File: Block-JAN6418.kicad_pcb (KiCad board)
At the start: 2 copper layers, 65 x 65 mm, 21 parts, among them J1 B+, J2 Sig_gnd, J3 Sig_in, J4 Sig_out, J5 9V, U1 JAN6418, U2 LM317L

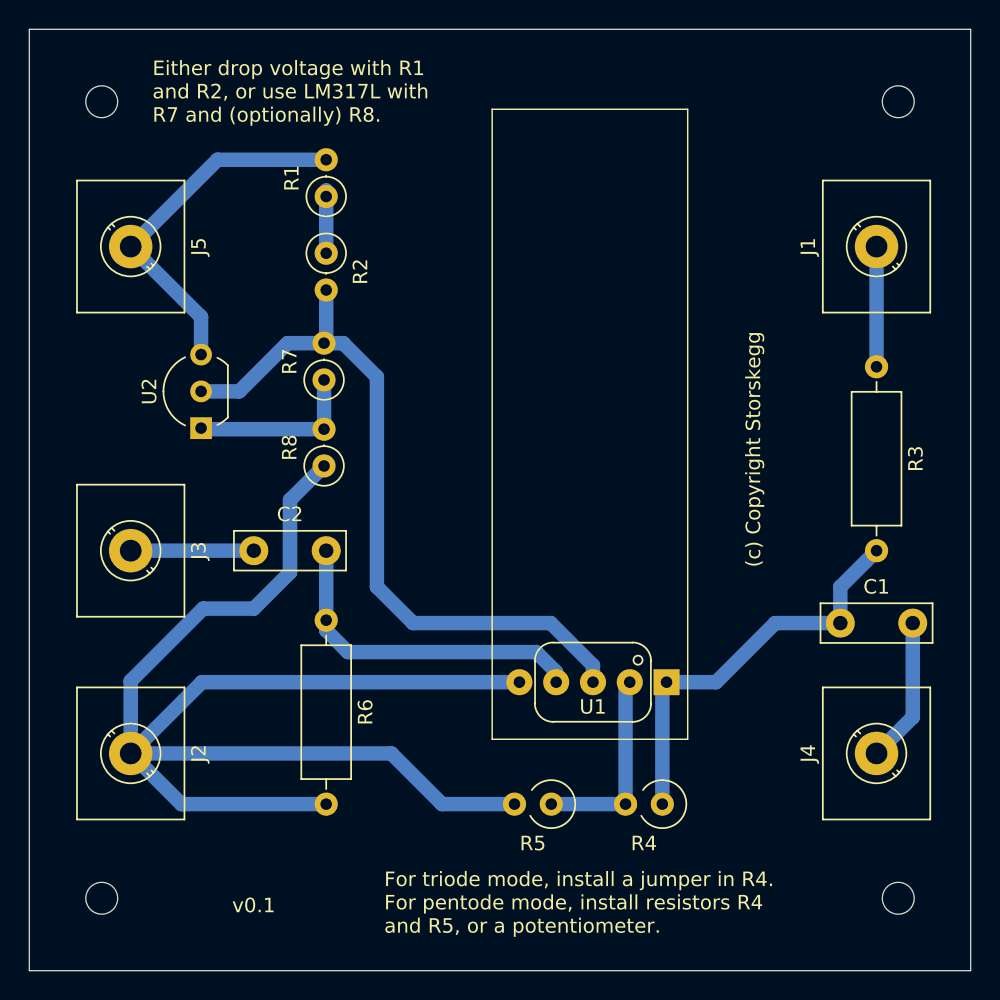
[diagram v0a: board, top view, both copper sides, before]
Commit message: narrow the board, and add some additional silkscreening
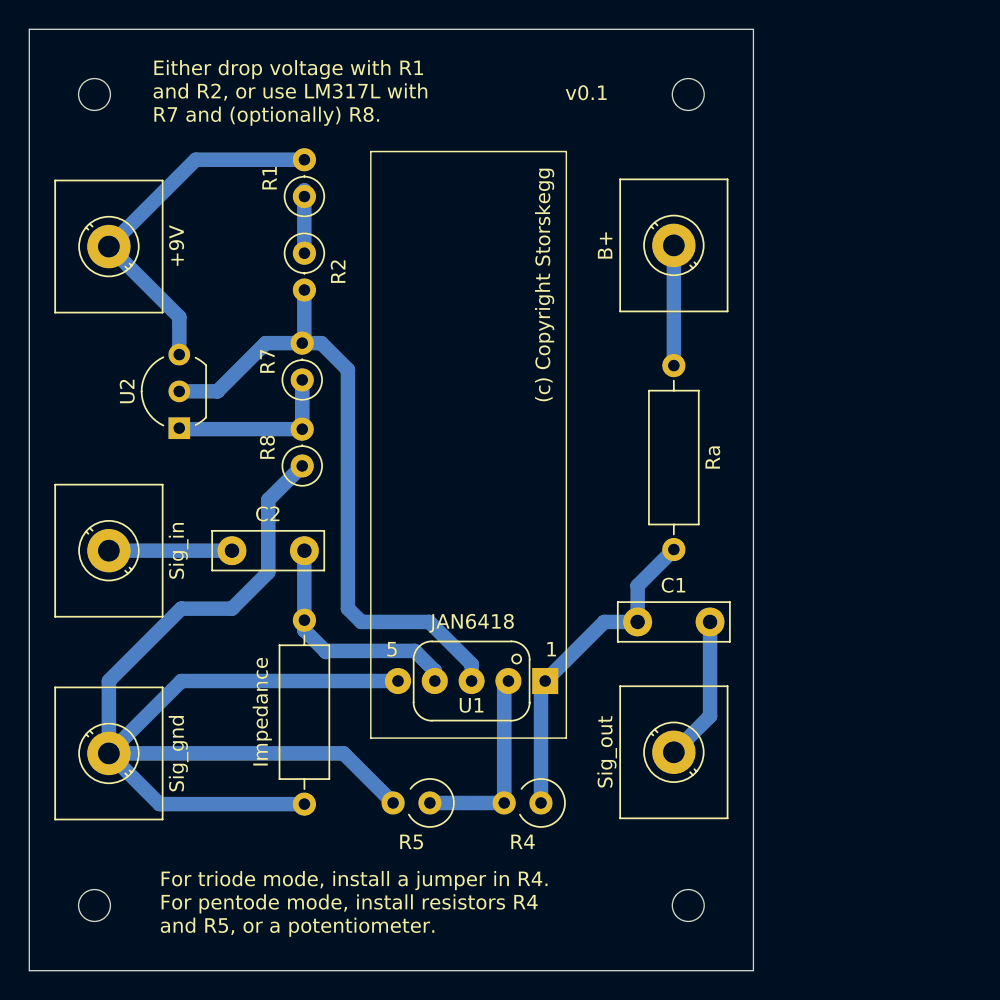
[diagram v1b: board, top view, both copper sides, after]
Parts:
- moved REF** 14.5 mm to (95.5, 39.5)
- moved REF** 14.5 mm to (95.5, 95.5)
- moved B+ 14.0 mm to (94.5, 49.9)
- moved C1 14.0 mm to (92.0, 75.9)
- moved Ra 14.0 mm to (94.5, 58.2)
- moved Sig_out 14.0 mm to (94.5, 84.9)
- moved R5 8.38 mm to (77.7, 88.4)
- moved R4 8.38 mm to (85.3, 88.4)
- moved U1 8.38 mm to (85.6, 80.0)
- moved +9V 1.51 mm to (55.5, 50.0)
- moved C2 1.51 mm to (64.0, 71.0)
- moved Sig_gnd 1.51 mm to (55.5, 85.0)
- moved Sig_in 1.51 mm to (55.5, 71.0)
- moved U2 1.51 mm to (60.4, 62.5)
- moved Impedance 1.50 mm to (69.0, 75.8)
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- renumbered J5 to +9V, J1 to B+, R6 to Impedance, R3 to Ra, J2 to Sig_gnd, J3 to Sig_in, J4 to Sig_out
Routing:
- net GND: track 99.2 -> 85.5 mm
- net Net-(U1A-G1): track 23.1 -> 16.2 mm
- net Net-(U2-VO): track 51.0 -> 45.3 mm
- net Net-(U1A-P): track 28.3 -> 22.7 mm
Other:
- board size 65 x 65 mm -> 50 x 65 mm
- board text added: "1"
- board text added: "5"
- board text added: "JAN6418"

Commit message: shrinkage
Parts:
- moved R8 6.45 mm to (62.5, 64.0)
- moved R7 5.80 mm to (63.5, 57.0), turned to 180 degrees
- moved U2 5.10 mm to (55.4, 61.5)
- moved R4 4.16 mm to (83.0, 85.0)
- moved R5 4.06 mm to (75.5, 85.0)
- moved R1 3.95 mm to (65.0, 46.5), turned to 180 degrees
- moved R2 3.95 mm to (65.0, 50.4)
- moved U1 3.04 mm to (83.0, 78.5)
- moved Impedance 2.66 mm to (67.5, 73.6)
- moved B+ 2.53 mm to (92.5, 48.4)
- moved C1 2.53 mm to (90.0, 74.4)
- moved Ra 2.53 mm to (92.5, 56.7)
- moved Sig_out 2.53 mm to (92.5, 83.4)
- moved C2 2.15 mm to (62.5, 69.5)
- moved REF** 2.12 mm to (94.0, 94.0)
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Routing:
- net +9V: track 25.5 -> 15.7 mm
- net GND: track 85.5 -> 76.4 mm
- net Net-(U1A-G2): track 13.7 -> 11.4 mm
- net Net-(U1A-G1): track 16.2 -> 14.7 mm
- net Net-(J3-Pin_1): track 8.50 -> 7.01 mm
- net Net-(U1A-P): track 22.7 -> 21.2 mm
- net Net-(U2-VO): track 45.3 -> 46.2 mm
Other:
- board size 50 x 65 mm -> 48 x 63 mm
- board text added: "Either drop voltage with R1 and R2, OR use LM317L with R7 and (optionally) R8."
- board text added: "v0.3"
- board text removed: "Either drop voltage with R1 and R2, or use LM317L with R7 and (optionally) R8."
- board text removed: "v0.1"

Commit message: bigger change...
1. Added L1 Ground Plane
2. Added filter and bandpass capacitors to LM317L optional block
3. `Sig_in` and `Sig_gnd` swapped physical locations...
    1. `Sig_gnd` is now closer to PSU block ground connections (lower
       impedance ground paths)
    2. `Sig_gnd` now closer to `R_impedance` ground connection
    3. `Sig_gnd` distance to `JAN6418` ground pin is about unchanged
4. Other general changes and general notes
    1. Valve heater power now routed further away from valve body
    2. Power blocks now a bit more compact, and further away from valve
       body
    3. No impeded ground paths on the ground plane (e.g. no going around
       vias, pins, etc; all straight line paths to `Sig_gnd`)
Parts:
- added C3: 100nF, Capacitor_THT:C_Rect_L4.6mm_W2.0mm_P2.50mm_MKS02_FKP02, F.Cu at (53.0, 61.8)
- added C4: 1uF, Capacitor_THT:CP_Radial_D4.0mm_P1.50mm, F.Cu at (58.0, 62.3)
- moved C2 16.5 mm to (62.5, 86.0)
- moved Sig_in 14.0 mm to (55.5, 83.5)
- moved Sig_gnd 12.5 mm to (55.5, 71.0)
- moved Impedance 9.58 mm to (65.0, 82.8), turned to 90 degrees
- moved U2 5.11 mm to (58.0, 57.1), turned to 180 degrees
- moved R2 1.67 mm to (64.5, 52.0), turned to 180 degrees
- moved R1 1.63 mm to (64.5, 48.0)
- moved R7 1.59 mm to (63.5, 58.5), turned to 90 degrees
- moved R8 1.00 mm to (63.5, 64.0)
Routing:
- net GND: track 76.4 -> 0.00 mm
- net Net-(U2-VO): track 46.2 -> 53.4 mm
- net +9V: track 15.7 -> 20.4 mm
- net Net-(U2-ADJ): track 12.0 -> 9.00 mm
- net Net-(U1A-G1): track 14.7 -> 16.2 mm
- net Net-(J3-Pin_1): track 7.01 -> 8.04 mm
- added copper zone on F.Cu, net GND
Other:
- board text added: "v0.5a"
- board text removed: "v0.3"

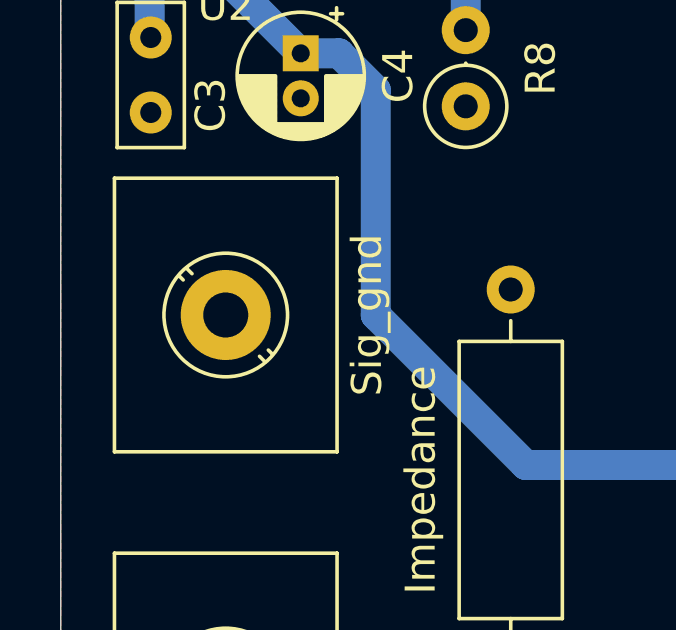
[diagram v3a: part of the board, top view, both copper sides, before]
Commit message: lower impedance of sig_gnd connection
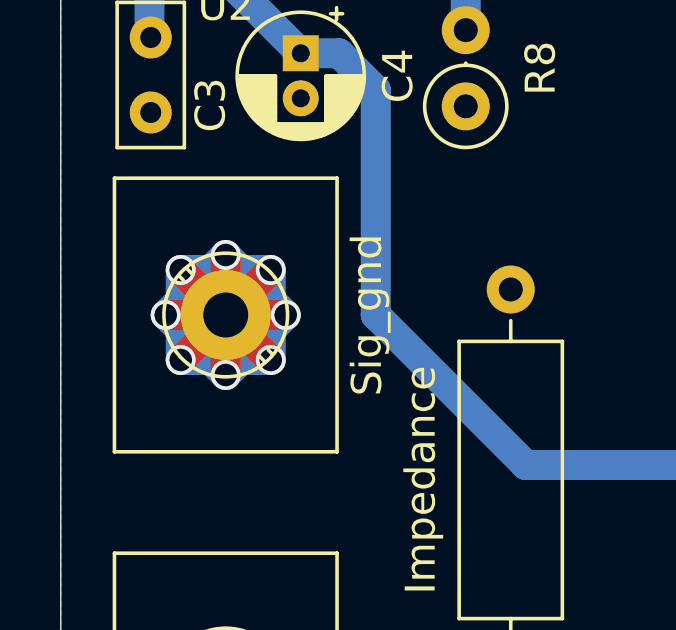
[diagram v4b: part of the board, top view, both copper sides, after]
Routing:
- net GND: track 0.00 -> 30.1 mm, vias 0 -> 8
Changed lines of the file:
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@@
+	)
+	(segment
+		(start 55.5 71)
+		(end 55.5 73)
+		(width 1)
+		(layer "F.Cu")
+		(net 6)
+	)
+	(segment
+		(start 55.5 71)
+		(end 54 72.5)
+		(width 1)
+		(layer "F.Cu")
+		(net 6)
+	)
+	(segment
+		(start 55.5 71)
+		(end 57 72.5)
+		(width 1)
+		(layer "F.Cu")
+		(net 6)
+	)
+	(segment
+		(start 55.5 71)
+		(end 57.5 71)
+		(width 1)
+		(layer "F.Cu")
+		(net 6)
+	)
+	(segment
+		(start 55.5 71)
+		(end 55.5 69)
+		(width 1)
+		(layer "F.Cu")
+		(net 6)
+	)
+	(segment
+		(start 55.5 71)
+		(end 54 69.5)
+		(width 1)
+		(layer "F.Cu")
+		(net 6)
+	)
+	(segment
+		(start 55.5 71)
+		(end 53.5 71)
+		(width 1)
+		(layer "F.Cu")
+		(net 6)
+	)
+	(segment
+		(start 55.5 71)
+		(end 57 69.5)
+		(width 1)
+		(layer "F.Cu")
+		(net 6)
+	)
+	(via
+		(at 55.5 73)
+		(size 1)
+		(drill 0.75)
+		(layers "F.Cu" "B.Cu")
+		(free yes)
+		(net 6)
+	)
+	(via
+		(at 57 69.5)
+		(size 1)
+		(drill 0.75)
+		(layers "F.Cu" "B.Cu")
+		(free yes)
+		(net 6)
+	)
+	(via
+		(at 55.5 69)
+		(size 1)
+		(drill 0.75)
+		(layers "F.Cu" "B.Cu")
+		(free yes)
+		(net 6)
+	)
+	(via
+		(at 54 69.5)
+		(size 1)
+		(drill 0.75)
+		(layers "F.Cu" "B.Cu")
+		(free yes)
+		(net 6)
+	)
+	(via
+		(at 57 72.5)
+		(size 1)
+		(drill 0.75)
+		(layers "F.Cu" "B.Cu")
+		(free yes)
+		(net 6)
+	)
+	(via
+		(at 54 72.5)
+		(size 1)
+		(drill 0.75)
+		(layers "F.Cu" "B.Cu")
+		(free yes)
+		(net 6)
+	)
+	(via
+		(at 57.5 71)
+		(size 1)
+		(drill 0.75)
+		(layers "F.Cu" "B.Cu")
+		(free yes)
+		(net 6)
+	)
+	(via
+		(at 53.5 71)
+		(size 1)
+		(drill 0.75)
+		(layers "F.Cu" "B.Cu")
+		(free yes)
+		(net 6)
+	)
+	(segment
+		(start 57 72.5)
+		(end 56 72.5)
+		(width 1)
+		(layer "B.Cu")
+		(net 6)
+	)
+	(segment
+		(start 55 69.5)
+		(end 55.5 69)
+		(width 1)
+		(layer "B.Cu")
+		(net 6)
+	)
+	(segment
+		(start 57 71.5)
+		(end 57.5 71)
+		(width 1)
+		(layer "B.Cu")
+		(net 6)
+	)
+	(segment
+		(start 54 71.5)
+		(end 53.5 71)
+		(width 1)
+		(layer "B.Cu")
+		(net 6)
+	)
+	(segment
+		(start 54 69.5)
+		(end 54 70.5)
+		(width 1)
+		(layer "B.Cu")
+		(net 6)
+	)
+	(segment
+		(start 57 70.5)
+		(end 57.5 71)
+		(width 1)
+		(layer "B.Cu")
+		(net 6)
+	)
+	(segment
+		(start 57 69.5)
+		(end 57 70.5)
+		(width 1)
+		(layer "B.Cu")
+		(net 6)
+	)
+	(segment
+		(start 54 72.5)
+		(end 55 72.5)
+		(width 1)
+		(layer "B.Cu")
+		(net 6)
+	)
+	(segment
+		(start 54 69.5)
+		(end 55 69.5)
+		(width 1)
+		(layer "B.Cu")
+		(net 6)
+	)
+	(segment
+		(start 57 72.5)
+		(end 57 71.5)
+		(width 1)
+		(layer "B.Cu")
+		(net 6)
+	)
+	(segment
+		(start 57 69.5)
+		(end 56 69.5)
+		(width 1)
+		(layer "B.Cu")
+		(net 6)
+	)
+	(segment
+		(start 55 72.5)
+		(end 55.5 73)
+		(width 1)
+		(layer "B.Cu")
+		(net 6)
+	)
+	(segment
+		(start 56 72.5)
+		(end 55.5 73)
+		(width 1)
+		(layer "B.Cu")
+		(net 6)
+	)
+	(segment
+		(start 54 70.5)
+		(end 53.5 71)
+		(width 1)
+		(layer "B.Cu")
+		(net 6)
+	)
+	(segment
+		(start 54 72.5)
+		(end 54 71.5)
+		(width 1)
+		(layer "B.Cu")
+		(net 6)
+	)
+	(segment
+		(start 56 69.5)
+		(end 55.5 69)
+		(width 1)
+		(layer "B.Cu")
+		(net 6)
 	)
 	(segment
